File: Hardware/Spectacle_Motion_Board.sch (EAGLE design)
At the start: 47 parts, among them J1 FTDI_DEVICE, J10 AUDIO-JACK3, J3 USB-MICROB, J4 AUDIO-JACK3, U1 CY8C4146LQI-S422, U2 3.3V/150mA

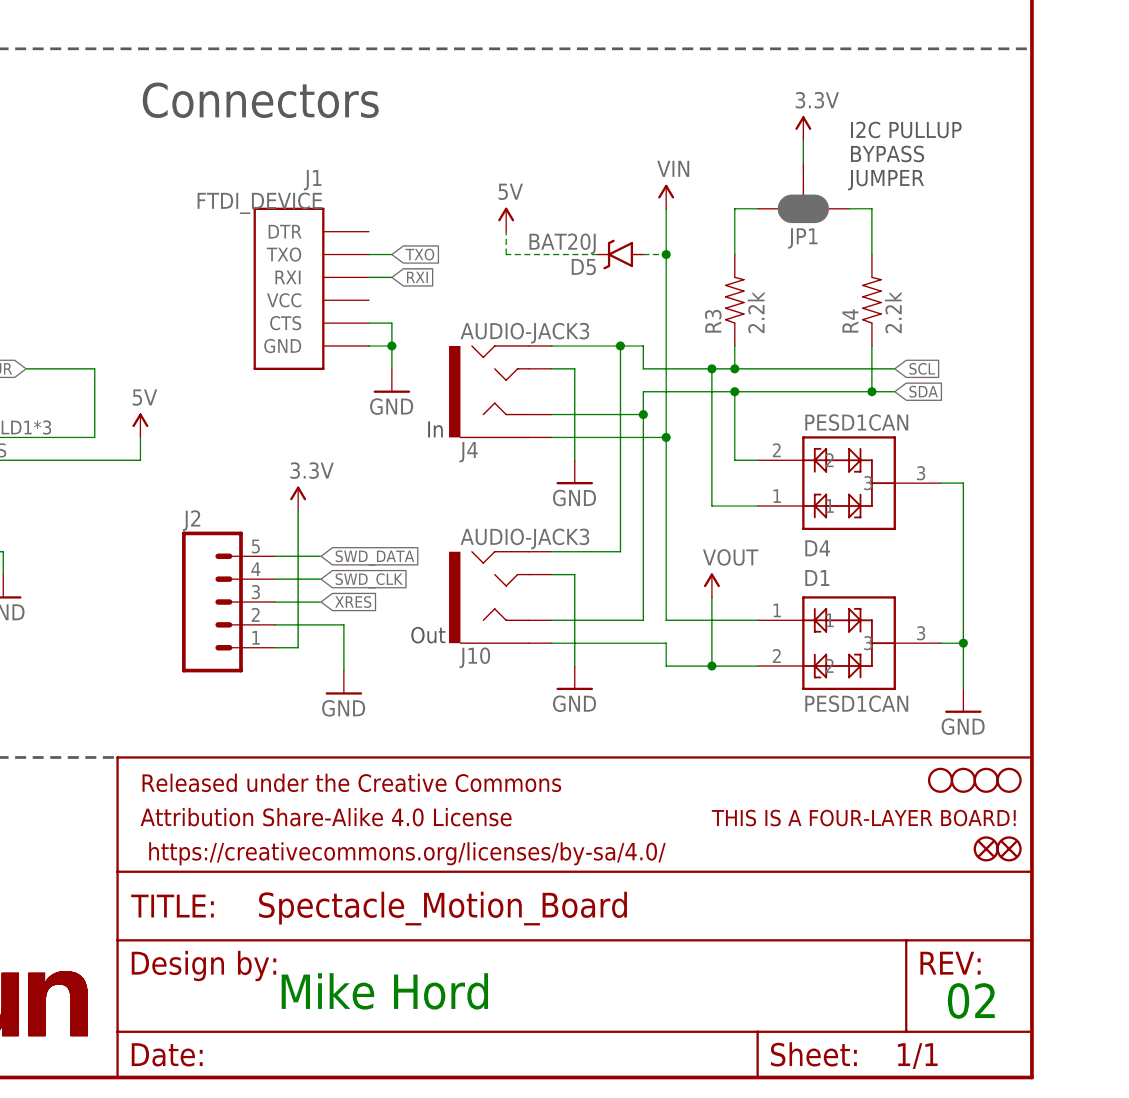
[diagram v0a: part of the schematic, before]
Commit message: Feedback from review incorporated, ready for qc review
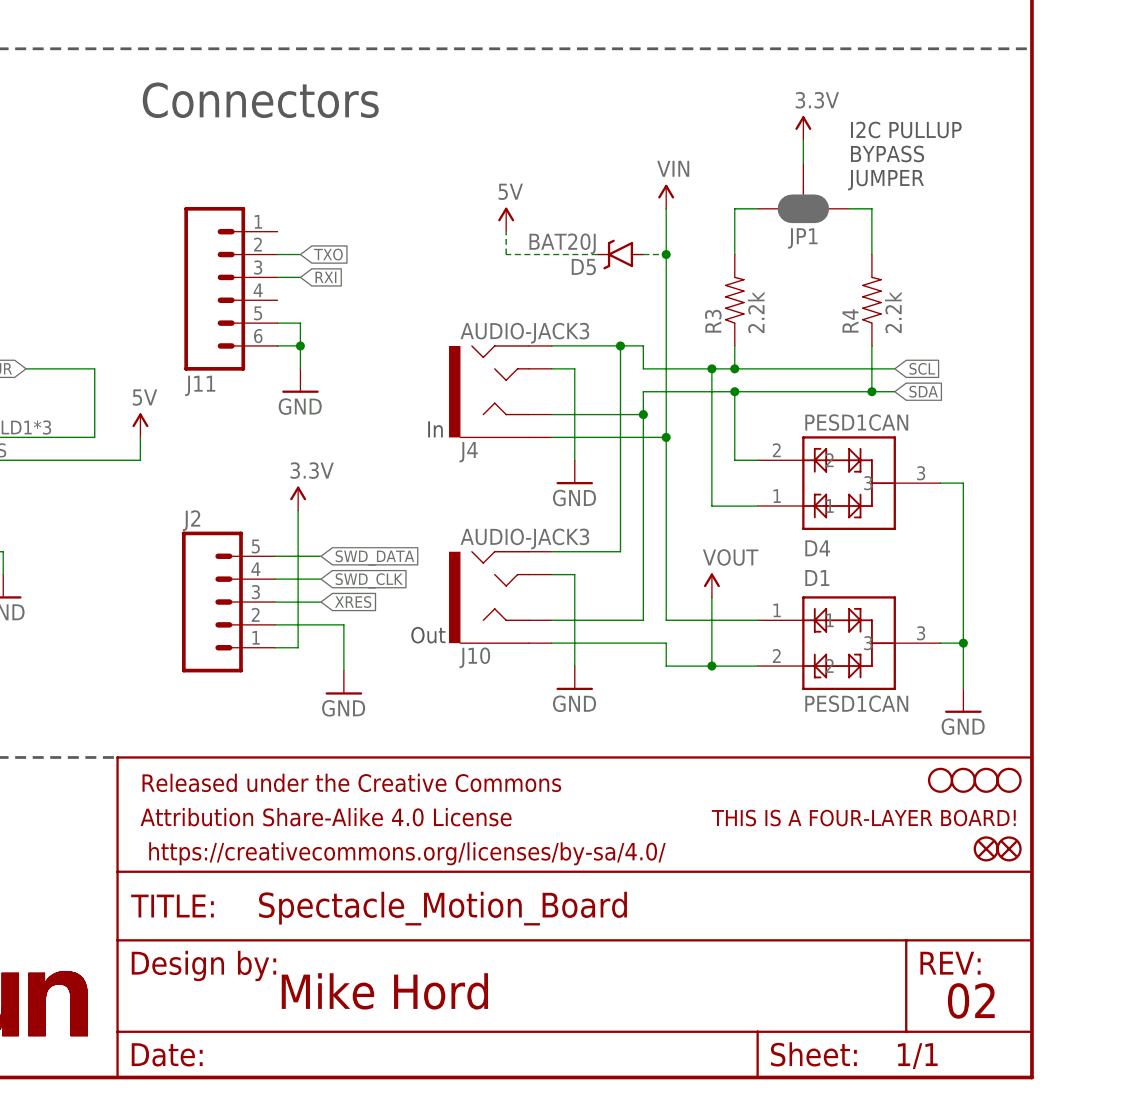
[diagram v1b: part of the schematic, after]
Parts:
- removed J1: FTDI_DEVICE, SparkFun-Connectors:FTDI_DEVICE
- added J11: (no value), SparkFun-Connectors:M06NO_SILK_FEMALE_PTH
- J2: device SparkFun-Connectors:M05PTH -> SparkFun-Connectors:M05NO_SILK
- J3: device SparkFun-Connectors:USB-MICROB" -> SparkFun-Connectors:USB-MICROBREDUCED_PASTE
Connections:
- net GND: now also J11.5, J11.6; no longer J1.CTS, J1.GND
- net RXI: now also J11.3; no longer J1.RXI
- net TXO: now also J11.2; no longer J1.TXO
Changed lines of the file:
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@@
 <part name="R4" library="SparkFun-Resistors" deviceset="2.2KOHM-1/10W-1%(0603)" device="" value="2.2k"/>
 <part name="JP1" library="SparkFun-Passives" deviceset="JUMPER-PAD-3-NC_BY_PASTE" device=""/>
-<part name="J2" library="SparkFun-Connectors" deviceset="M05" device="PTH"/>
+<part name="J2" library="SparkFun-Connectors" deviceset="M05" device="NO_SILK"/>
 <part name="GND10" library="SparkFun-Aesthetics" deviceset="GND" device=""/>
-<part name="J1" library="SparkFun-Connectors" deviceset="FTDI_DEVICE" device=""/>
 <part name="GND11" library="SparkFun-Aesthetics" deviceset="GND" device=""/>
 <part name="D2" library="SparkFun-LED" deviceset="LED-RED" device="0603" value="RED"/>
@@
 <part name="H3" library="SparkFun-Electromechanical" deviceset="STAND-OFF" device=""/>
 <part name="H4" library="SparkFun-Electromechanical" deviceset="STAND-OFF" device=""/>
-<part name="J3" library="SparkFun-Connectors" deviceset="USB-MICROB" device="&quot;" value="USB-MICROB"/>
+<part name="J3" library="SparkFun-Connectors" deviceset="USB-MICROB" device="REDUCED_PASTE" value="USB-MICROB"/>
 <part name="SUPPLY12" library="SparkFun-Aesthetics" deviceset="5V" device=""/>
 <part name="GND2" library="SparkFun-Aesthetics" deviceset="GND" device=""/>
@@
 <part name="R8" library="SparkFun-Resistors" deviceset="10KOHM-1/10W-1%(0603)" device="0603" value="10K"/>
 <part name="U$5" library="SparkFun-Aesthetics" deviceset="VOUT" device=""/>
+<part name="J11" library="SparkFun-Connectors" deviceset="M06" device="NO_SILK_FEMALE_PTH"/>
 </parts>
 <sheets>
@@
 <wire x1="106.68" y1="185.42" x2="106.68" y2="114.3" width="0.3048" layer="97" style="longdash"/>
 <wire x1="66.04" y1="86.36" x2="0" y2="86.36" width="0.3048" layer="97" style="longdash"/>
-<text x="165.1" y="7.62" size="3.81" layer="91" font="vector">Mike Hord</text>
-<text x="239.268" y="6.604" size="3.81" layer="91" font="vector">02</text>
+<text x="165.1" y="7.62" size="3.81" layer="94" font="vector">Mike Hord</text>
+<text x="239.268" y="6.604" size="3.81" layer="94" font="vector">02</text>
 <wire x1="106.68" y1="114.3" x2="248.92" y2="114.3" width="0.3048" layer="97" style="longdash"/>
 <text x="109.22" y="116.84" size="3.81" layer="97" font="vector">MCU</text>
@@
 <instance part="J2" gate="G$1" x="157.226" y="52.832"/>
 <instance part="GND10" gate="1" x="172.466" y="42.672"/>
-<instance part="J1" gate="G$1" x="170.18" y="88.9" rot="MR0"/>
-<instance part="GND11" gate="1" x="177.8" y="76.2"/>
+<instance part="GND11" gate="1" x="167.64" y="76.2"/>
 <instance part="D2" gate="G$1" x="88.9" y="129.54"/>
 <instance part="SW1" gate="G$1" x="45.72" y="147.32"/>
@@
 <instance part="R8" gate="G$1" x="101.6" y="58.42" rot="R90"/>
 <instance part="U$5" gate="G$1" x="213.36" y="53.34"/>
+<instance part="J11" gate="G$1" x="160.02" y="88.9" rot="MR180"/>
 </instances>
 <busses>
@@
 </segment>
 <segment>
-<pinref part="J1" gate="G$1" pin="GND"/>
 <pinref part="GND11" gate="1" pin="GND"/>
-<wire x1="175.26" y1="81.28" x2="177.8" y2="81.28" width="0.1524" layer="91"/>
-<wire x1="177.8" y1="81.28" x2="177.8" y2="78.74" width="0.1524" layer="91"/>
-<pinref part="J1" gate="G$1" pin="CTS"/>
-<wire x1="175.26" y1="83.82" x2="177.8" y2="83.82" width="0.1524" layer="91"/>
-<wire x1="177.8" y1="83.82" x2="177.8" y2="81.28" width="0.1524" layer="91"/>
-<junction x="177.8" y="81.28"/>
+<wire x1="165.1" y1="81.28" x2="167.64" y2="81.28" width="0.1524" layer="91"/>
+<wire x1="167.64" y1="81.28" x2="167.64" y2="78.74" width="0.1524" layer="91"/>
+<wire x1="165.1" y1="83.82" x2="167.64" y2="83.82" width="0.1524" layer="91"/>
+<wire x1="167.64" y1="83.82" x2="167.64" y2="81.28" width="0.1524" layer="91"/>
+<junction x="167.64" y="81.28"/>
+<pinref part="J11" gate="G$1" pin="5"/>
+<pinref part="J11" gate="G$1" pin="6"/>
 </segment>
 <segment>
@@
 <net name="TXO" class="0">
 <segment>
-<pinref part="J1" gate="G$1" pin="TXO"/>
-<wire x1="175.26" y1="91.44" x2="177.8" y2="91.44" width="0.1524" layer="91"/>
-<label x="177.8" y="91.44" size="1.27" layer="95" xref="yes"/>
+<wire x1="165.1" y1="91.44" x2="167.64" y2="91.44" width="0.1524" layer="91"/>
+<label x="167.64" y="91.44" size="1.27" layer="95" xref="yes"/>
+<pinref part="J11" gate="G$1" pin="2"/>
 </segment>
 <segment>
@@
 <net name="RXI" class="0">
 <segment>
-<pinref part="J1" gate="G$1" pin="RXI"/>
-<wire x1="175.26" y1="88.9" x2="177.8" y2="88.9" width="0.1524" layer="91"/>
-<label x="177.8" y="88.9" size="1.27" layer="95" xref="yes"/>
-</segment>
-<segment>
+<wire x1="165.1" y1="88.9" x2="167.64" y2="88.9" width="0.1524" layer="91"/>
+<label x="167.64" y="88.9" size="1.27" layer="95" xref="yes"/>
+<pinref part="J11" gate="G$1" pin="3"/>
+</segment>
+<segment>

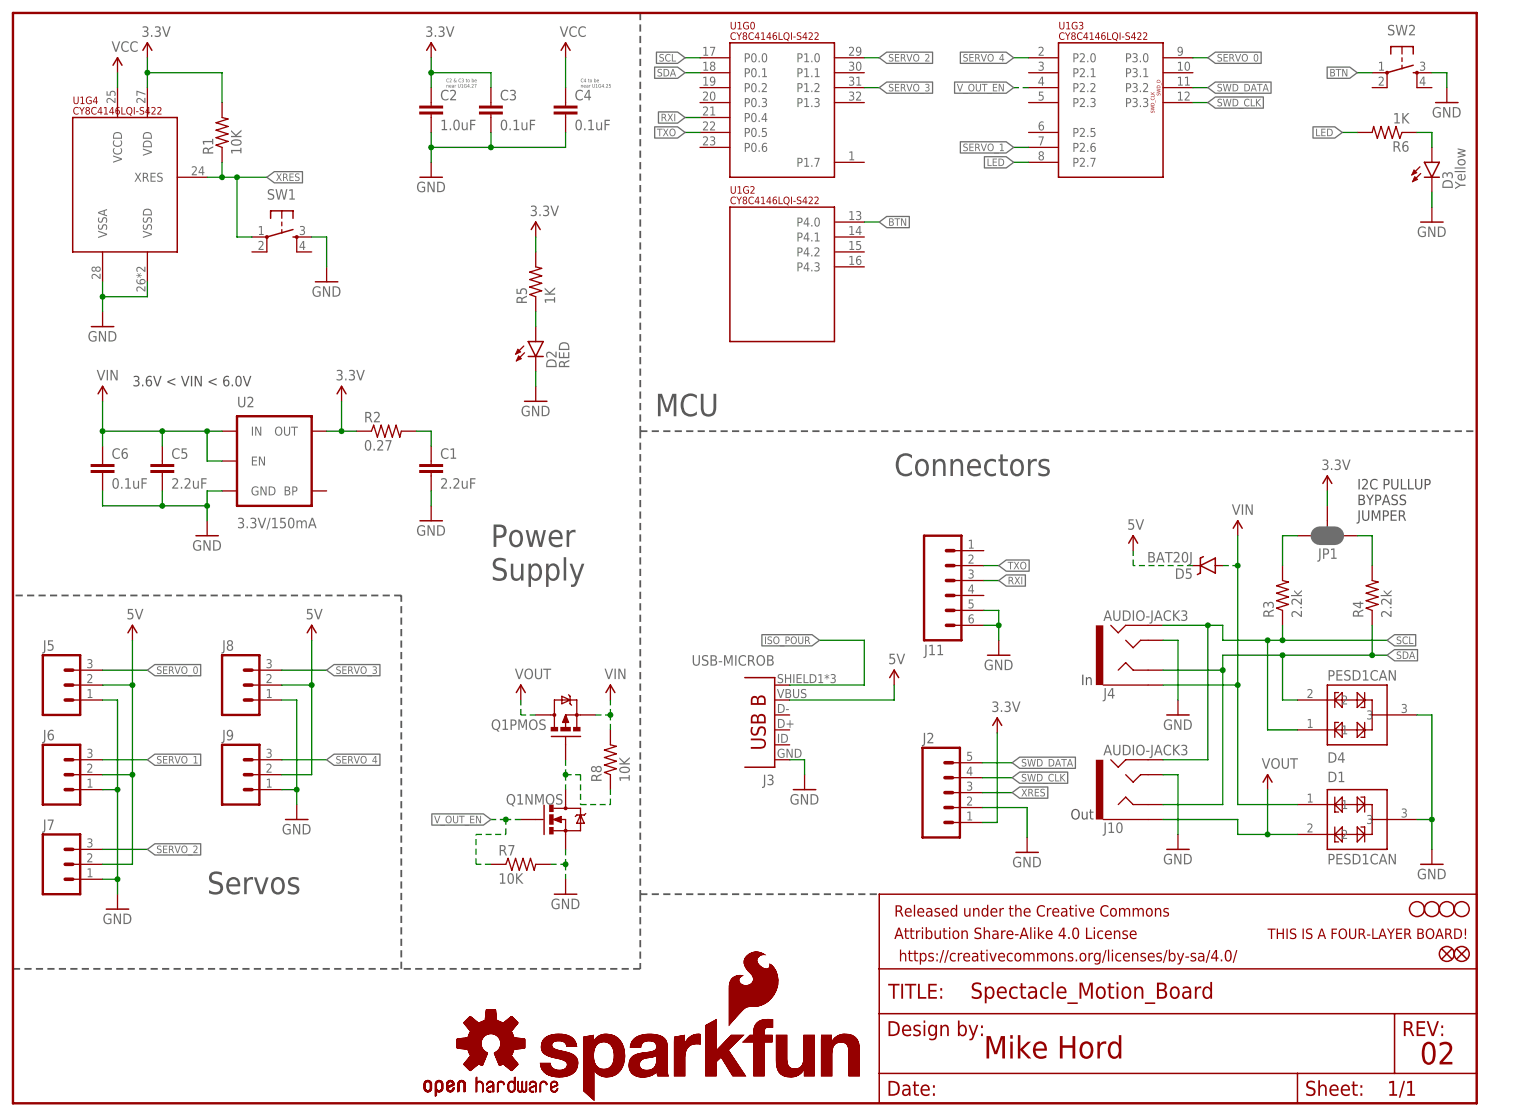
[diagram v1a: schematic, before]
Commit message: Chg I2C pullup value
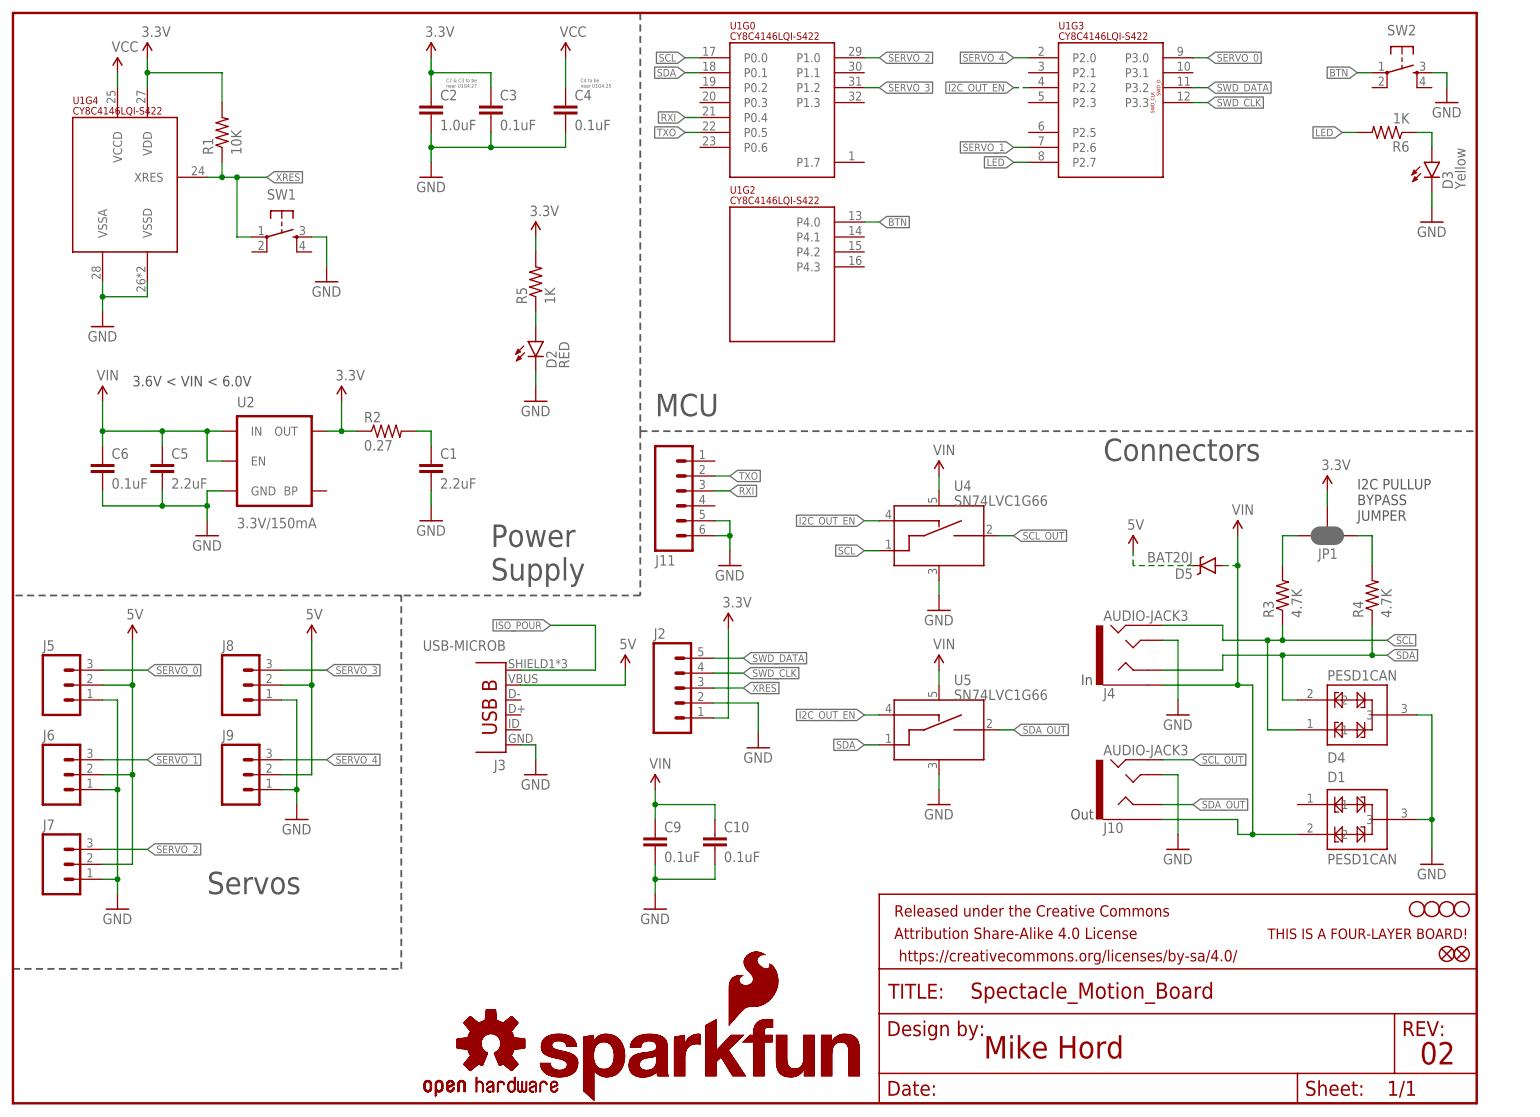
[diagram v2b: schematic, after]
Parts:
- removed Q1: (no value), SparkFun-DiscreteSemi:IRF7509
- removed R7, R8: 10K, SparkFun-Resistors:10KOHM-1/10W-1%(0603)0603
- added C10, C9: 0.1uF, SparkFun-Capacitors:0.1UF-16V(+-10%)(0402)
- added U4, U5: SN74LVC1G66, SparkFun-AnalogIC:SN74LVC1G66_SPST_AMUX
- R3, R4: value 2.2k -> 4.7K; device SparkFun-Resistors:2.2KOHM-1/10W-1%(0603) -> SparkFun-Resistors:4.7KOHM-1/10W-1%(0603)
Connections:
- removed net N$26: Q1NMOS.D, Q1PMOS.G, R8.1
- removed net VOUT: D1.2, J10.EARTH, Q1PMOS.D
- removed net V_OUT_EN: Q1NMOS.G, R7.1, U1G3.P2.2
- new net I2C_OUT_EN: U1G3.P2.2, U4.CTRL_IN, U5.CTRL_IN
- new net SCL_OUT: J10.RING2, U4.A_OUT
- new net SDA_OUT: J10.RING1, U5.A_OUT
- net GND: now also C10.2, C9.2, U4.VSS, U5.VSS; no longer Q1NMOS.S, R7.2
- net SCL: now also U4.A_IN; no longer J10.RING2
- net SDA: now also U5.A_IN; no longer J10.RING1
- net VIN: now also C10.1, C9.1, D1.2, J10.EARTH, U4.VCC, U5.VCC; no longer D1.1, Q1PMOS.S, R8.2
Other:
- moved on the sheet: J11, J2, J3

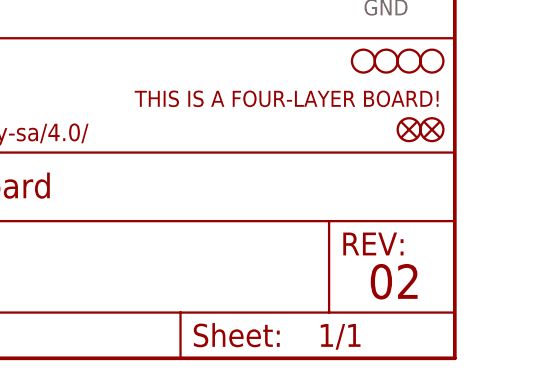
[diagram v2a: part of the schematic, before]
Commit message: Feedback from reviews incorporated
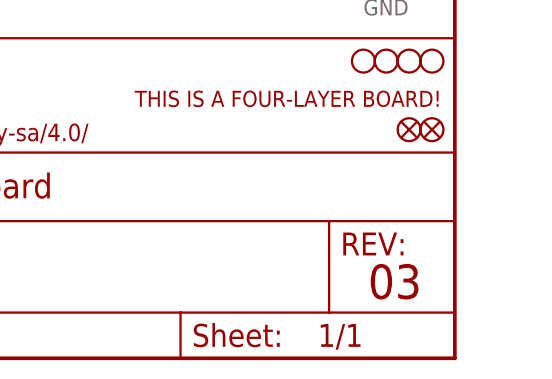
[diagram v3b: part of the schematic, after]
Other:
- note added: "03"
- note removed: "02"
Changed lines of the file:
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@@
 <wire x1="66.04" y1="86.36" x2="0" y2="86.36" width="0.3048" layer="97" style="longdash"/>
 <text x="165.1" y="7.62" size="3.81" layer="94" font="vector">Mike Hord</text>
-<text x="239.268" y="6.604" size="3.81" layer="94" font="vector">02</text>
+<text x="239.268" y="6.604" size="3.81" layer="94" font="vector">03</text>
 <wire x1="106.68" y1="114.3" x2="248.92" y2="114.3" width="0.3048" layer="97" style="longdash"/>
 <text x="109.22" y="116.84" size="3.81" layer="97" font="vector">MCU</text>
